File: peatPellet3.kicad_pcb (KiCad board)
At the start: 2 copper layers, 87.6 x 56.5 mm, 63 parts, among them J1 Barrel_Jack_Switch, J2 AudioJack2, J3 AudioJack2, K1 Relay_DPDT, SW1 SW_SPDT, SW2 SW_SPDT, SW3 SW_SPDT_MSM, U1 TL072, U2 L78L05_SO8, U3 LM555xM

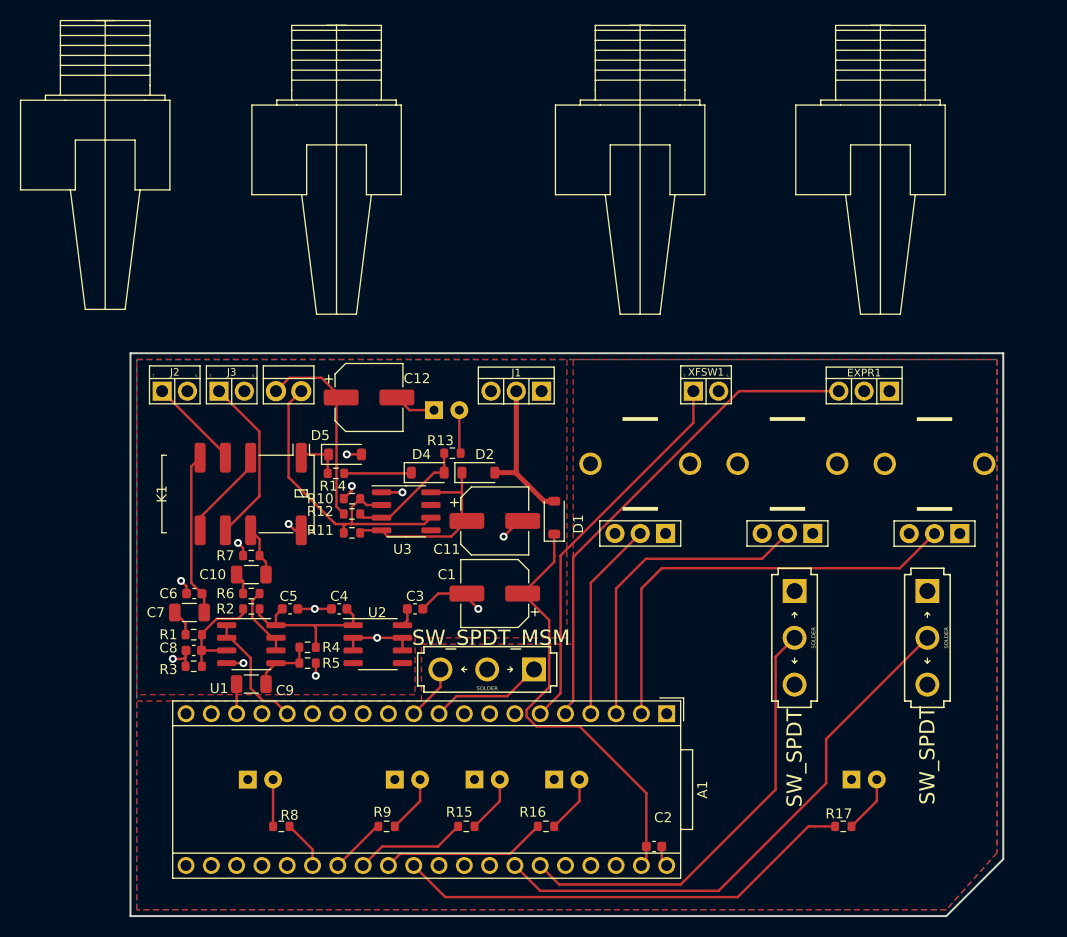
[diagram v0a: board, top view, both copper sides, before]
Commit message: 5v pour added
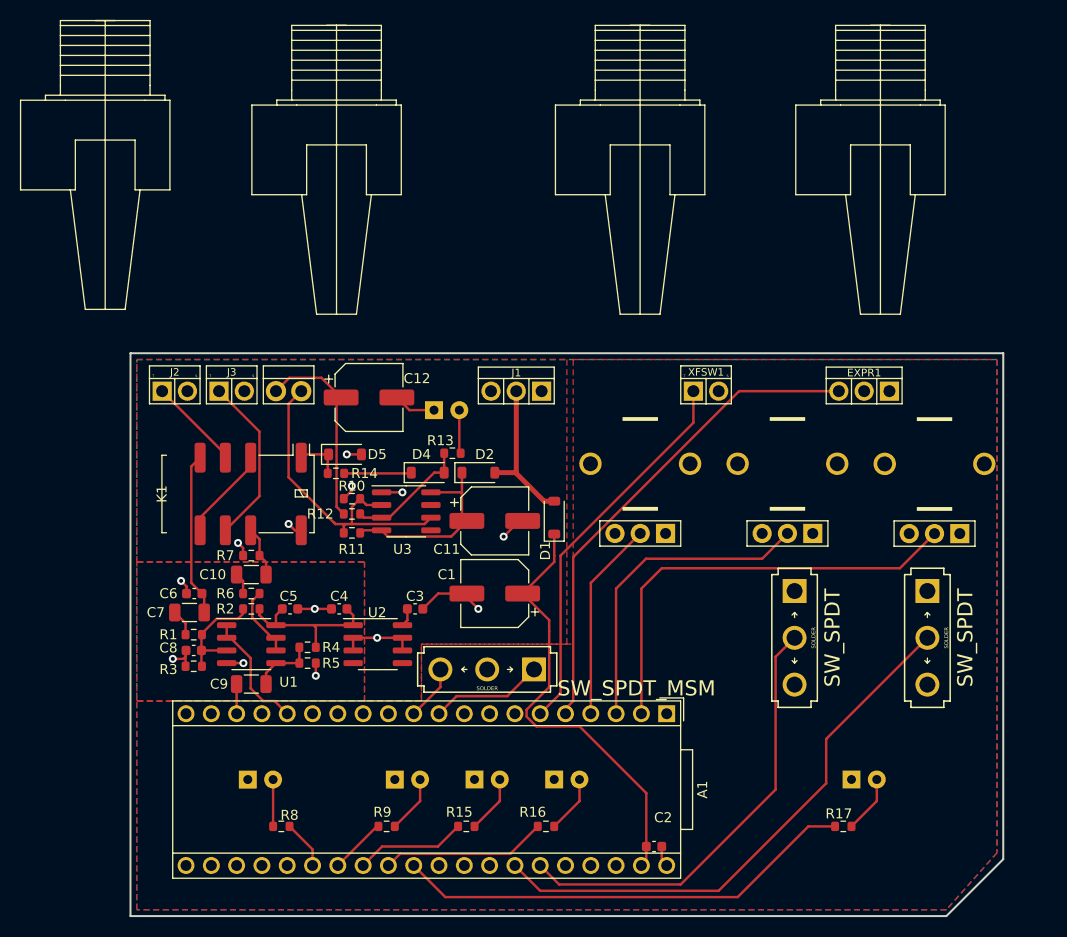
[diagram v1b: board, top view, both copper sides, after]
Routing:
- net GND: track 43.3 -> 42.4 mm
- added copper zone on F.Cu, net +5V
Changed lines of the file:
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@@
     (property "ki_keywords" "R res resistor")
     (attr smd)
-    (fp_text reference "R14" (at -0.305 1.27) (layer "F.SilkS")
+    (fp_text reference "R14" (at 2.87 0) (layer "F.SilkS")
         (effects (font (size 1 1) (thickness 0.15)))
     )
@@
     (property "ki_keywords" "diode Schottky")
     (attr smd)
-    (fp_text reference "D1" (at -0.635 2.425 90) (layer "F.SilkS")
+    (fp_text reference "D1" (at -3.33 -0.895 90) (layer "F.SilkS")
         (effects (font (size 1 1) (thickness 0.15)))
     )
@@
     (property "ki_keywords" "R res resistor")
     (attr smd)
-    (fp_text reference "R11" (at 3.185 0.26) (layer "F.SilkS")
+    (fp_text reference "R11" (at 0.01 -1.645) (layer "F.SilkS")
         (effects (font (size 1 1) (thickness 0.15)))
     )
@@
         (effects (font (size 1.2065 1.2065) (thickness 0.127)) (justify left top mirror))
     )
-    (fp_text value "SW_SPDT_MSM" (at -3.175 -0.381 -360) (layer "F.SilkS")
+    (fp_text value "SW_SPDT_MSM" (at 1.905 -14.986 -360) (layer "F.SilkS")
         (effects (font (size 1.524 1.524) (thickness 0.15)))
     )
@@
         (effects (font (size 1.2065 1.2065) (thickness 0.127)) (justify left top mirror))
     )
-    (fp_text value "SW_SPDT" (at 0 12.065 -90) (layer "F.SilkS")
+    (fp_text value "SW_SPDT" (at 3.81 0 -90) (layer "F.SilkS")
         (effects (font (size 1.524 1.524) (thickness 0.15)))
     )
@@
     (property "ki_keywords" "R res resistor")
     (attr smd)
-    (fp_text reference "R10" (at 3.185 0) (layer "F.SilkS")
+    (fp_text reference "R10" (at 0.01 1.27) (layer "F.SilkS")
         (effects (font (size 1 1) (thickness 0.15)))
     )
@@
         (effects (font (size 1.2065 1.2065) (thickness 0.127)) (justify left top mirror))
     )
-    (fp_text value "SW_SPDT" (at 0 11.811 90) (layer "F.SilkS")
+    (fp_text value "SW_SPDT" (at 3.81 0 90) (layer "F.SilkS")
         (effects (font (size 1.524 1.524) (thickness 0.15)))
     )
@@
         (effects (font (size 1 1) (thickness 0.15)))
     )
-    (fp_text value "L78L05_SO8" (at -0.065 4.445) (layer "F.Fab")
+    (fp_text value "L78L05_SO8" (at -0.065 -1.27) (layer "F.Fab")
         (effects (font (size 1 1) (thickness 0.15)))
     )
@@
     (property "ki_keywords" "cap capacitor")
     (attr smd)
-    (fp_text reference "C9" (at -3.38 -0.635) (layer "F.SilkS")
+    (fp_text reference "C9" (at 3.24 0) (layer "F.SilkS")
         (effects (font (size 1 1) (thickness 0.15)))
     )
-    (fp_text value "1u" (at -5.015 -0.635) (layer "F.Fab")
+    (fp_text value "1u" (at 0.065 0.2) (layer "F.Fab")
         (effects (font (size 1 1) (thickness 0.15)))
     )
@@
     (property "ki_keywords" "diode Schottky")
     (attr smd)
-    (fp_text reference "D5" (at -2.49 -1.905) (layer "F.SilkS")
+    (fp_text reference "D5" (at 3.225 0) (layer "F.SilkS")
         (effects (font (size 1 1) (thickness 0.15)))
     )
@@
     (property "ki_keywords" "R res resistor")
     (attr smd)
-    (fp_text reference "R12" (at 3.185 0.265) (layer "F.SilkS")
+    (fp_text reference "R12" (at 3.185 0) (layer "F.SilkS")
         (effects (font (size 1 1) (thickness 0.15)))
     )
@@
     (property "ki_keywords" "dual opamp")
     (attr smd)
-    (fp_text reference "U1" (at -3.24 4.445) (layer "F.SilkS")
+    (fp_text reference "U1" (at 3.745 3.81) (layer "F.SilkS")
         (effects (font (size 1 1) (thickness 0.15)))
     )
-    (fp_text value "TL072" (at -6.415 4.445) (layer "F.Fab")
+    (fp_text value "TL072" (at -0.065 -0.635) (layer "F.Fab")
         (effects (font (size 1 1) (thickness 0.15)))
     )
@@
   (segment (start 92.581751 114.935) (end 94.615 116.968249) (width 0.25) (layer "F.Cu") (net 13))
   (segment (start 93.205 119.58) (end 93.205 122.555) (width 0.25) (layer "F.Cu") (net 15))
-  (segment (start 109.855 114.935) (end 110.231751 114.935) (width 0.25) (layer "F.Cu") (net 17))
   (segment (start 98.425 103.505) (end 99.06 104.14) (width 0.25) (layer "F.Cu") (net 17))
   (segment (start 88.175 110.49) (end 88.175 109.765) (width 0.25) (layer "F.Cu") (net 17))
@@
   (segment (start 113.025 92.075) (end 110.565 92.075) (width 0.25) (layer "F.Cu") (net 17))
   (segment (start 116.32 110.49) (end 116.32 110.645) (width 0.25) (layer "F.Cu") (net 17))
-  (segment (start 117.475 112.03) (end 117.39 112.115) (width 0.25) (layer "F.Cu") (net 17))
   (segment (start 86.8 117.05) (end 87.865 117.05) (width 0.25) (layer "F.Cu") (net 17))
   (segment (start 87.865 117.05) (end 88.075 116.84) (width 0.25) (layer "F.Cu") (net 17))
@@
   (segment (start 104.905 114.935) (end 104.905 116.205) (width 0.25) (layer "F.Cu") (net 17))
   (segment (start 109.855 100.33) (end 107.76 100.33) (width 0.25) (layer "F.Cu") (net 17))
-  (segment (start 104.905 114.935) (end 105.281751 114.935) (width 0.25) (layer "F.Cu") (net 17))
   (segment (start 101.155 118.745) (end 101.155 117.475) (width 0.25) (layer "F.Cu") (net 17))
   (segment (start 93.8905 117.475) (end 92.205 117.475) (width 0.25) (layer "F.Cu") (net 17))
@@
   (segment (start 125.095 107.315) (end 125.095 106.68) (width 0.25) (layer "F.Cu") (net 66))
   (segment (start 134.34 135.89) (end 134.34 137.3) (width 0.25) (layer "F.Cu") (net 66))
+  (zone (net 45) (net_name "+5V") (layer "F.Cu") (hatch edge 0.5)
+    (priority 3)
+    (connect_pads (clearance 0.5))
+    (min_thickness 0.25) (filled_areas_thickness no)
+    (fill yes (thermal_gap 0.5) (thermal_bridge_width 0.5))
+    (polygon
+      (pts
+        (xy 106.045 121.285)
+        (xy 83.185 121.285)
+        (xy 83.185 107.315)
+        (xy 106.045 107.315)
+      )
+    )
+  )
   (zone (net 66) (net_name "+9V") (layer "F.Cu") (hatch edge 0.5)
     (priority 1)
@@
     (polygon
       (pts
+        (xy 126.365 115.57)
+        (xy 111.76 115.57)
+        (xy 111.76 121.285)
+        (xy 106.045 121.285)
+        (xy 106.045 107.315)
+        (xy 83.185 107.315)
         (xy 83.185 86.995)
         (xy 126.365 86.995)
-        (xy 126.365 114.935)
-        (xy 111.125 114.935)
-        (xy 111.125 120.65)
-        (xy 83.185 120.65)
       )
     )

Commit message: Last update for today, pours, zones, too much stuff to list
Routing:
- net +5V: track 16.5 -> 2.69 mm
- net +9V: track 66.1 -> 65.5 mm

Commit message: pours, traces, graphics
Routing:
- net +3.3VA: track 0.00 -> 159.2 mm
- net +9V: track 65.5 -> 31.6 mm
- net KNOB3: track 44.3 -> 45.1 mm
- removed copper zone on F.Cu, net +3.3VA
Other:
- board text added: "Be careful of the thought-seeds you plant in the garden of your mind For seeds grow after their kind"
- board text added: "Free your ass and your mind will follow Play on, children"
- board text added: "Good thoughts bring forth good fruit Bullshit thoughts rot your meat"
- board text added: "PEAT PELLET v1 for growing things"

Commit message: jumpers
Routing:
- net (no net): track 0.00 -> 7.60 mm
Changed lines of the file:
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@@
     )
     (stroke (width 0.2) (type solid)) (fill none) (layer "Edge.Cuts"))
-  (gr_text "Free your ass and your mind will follow\nPlay on, children" (at 87.63 127) (layer "F.SilkS")
+  (gr_text "Free your ass and your mind will follow\n                    Play on, children" (at 87.63 127) (layer "F.SilkS")
     (effects (font (size 1 1) (thickness 0.15)) (justify left bottom))
   )
@@
     (effects (font (size 1 1) (thickness 0.15)) (justify left bottom))
   )
+  (segment (start 122.555 121.285) (end 122.51 121.33) (width 0.25) (layer "F.Cu") (net 0))
+  (segment (start 122.51 121.33) (end 122.51 123.78) (width 0.25) (layer "F.Cu") (net 0))
+  (segment (start 107.27 121.33) (end 107.27 123.78) (width 0.25) (layer "F.Cu") (net 0))
+  (segment (start 122.51 123.78) (end 122.555 123.825) (width 0.25) (layer "F.Cu") (net 0))
+  (segment (start 109.81 121.33) (end 109.81 123.78) (width 0.25) (layer "F.Cu") (net 0))
+  (segment (start 107.315 121.285) (end 107.27 121.33) (width 0.25) (layer "F.Cu") (net 0))
+  (segment (start 109.855 121.285) (end 109.81 121.33) (width 0.25) (layer "F.Cu") (net 0))
   (segment (start 113.525 122.555) (end 115.287676 120.792324) (width 0.25) (layer "F.Cu") (net 6))
   (segment (start 115.287676 120.792324) (end 120.380676 120.792324) (width 0.25) (layer "F.Cu") (net 6))
